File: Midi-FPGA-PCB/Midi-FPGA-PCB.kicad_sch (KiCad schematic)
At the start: 18 parts, among them Q1 DMP2123L, SW1 Reset, U1 ESP32-WROOM-32, U2 AP7361EA

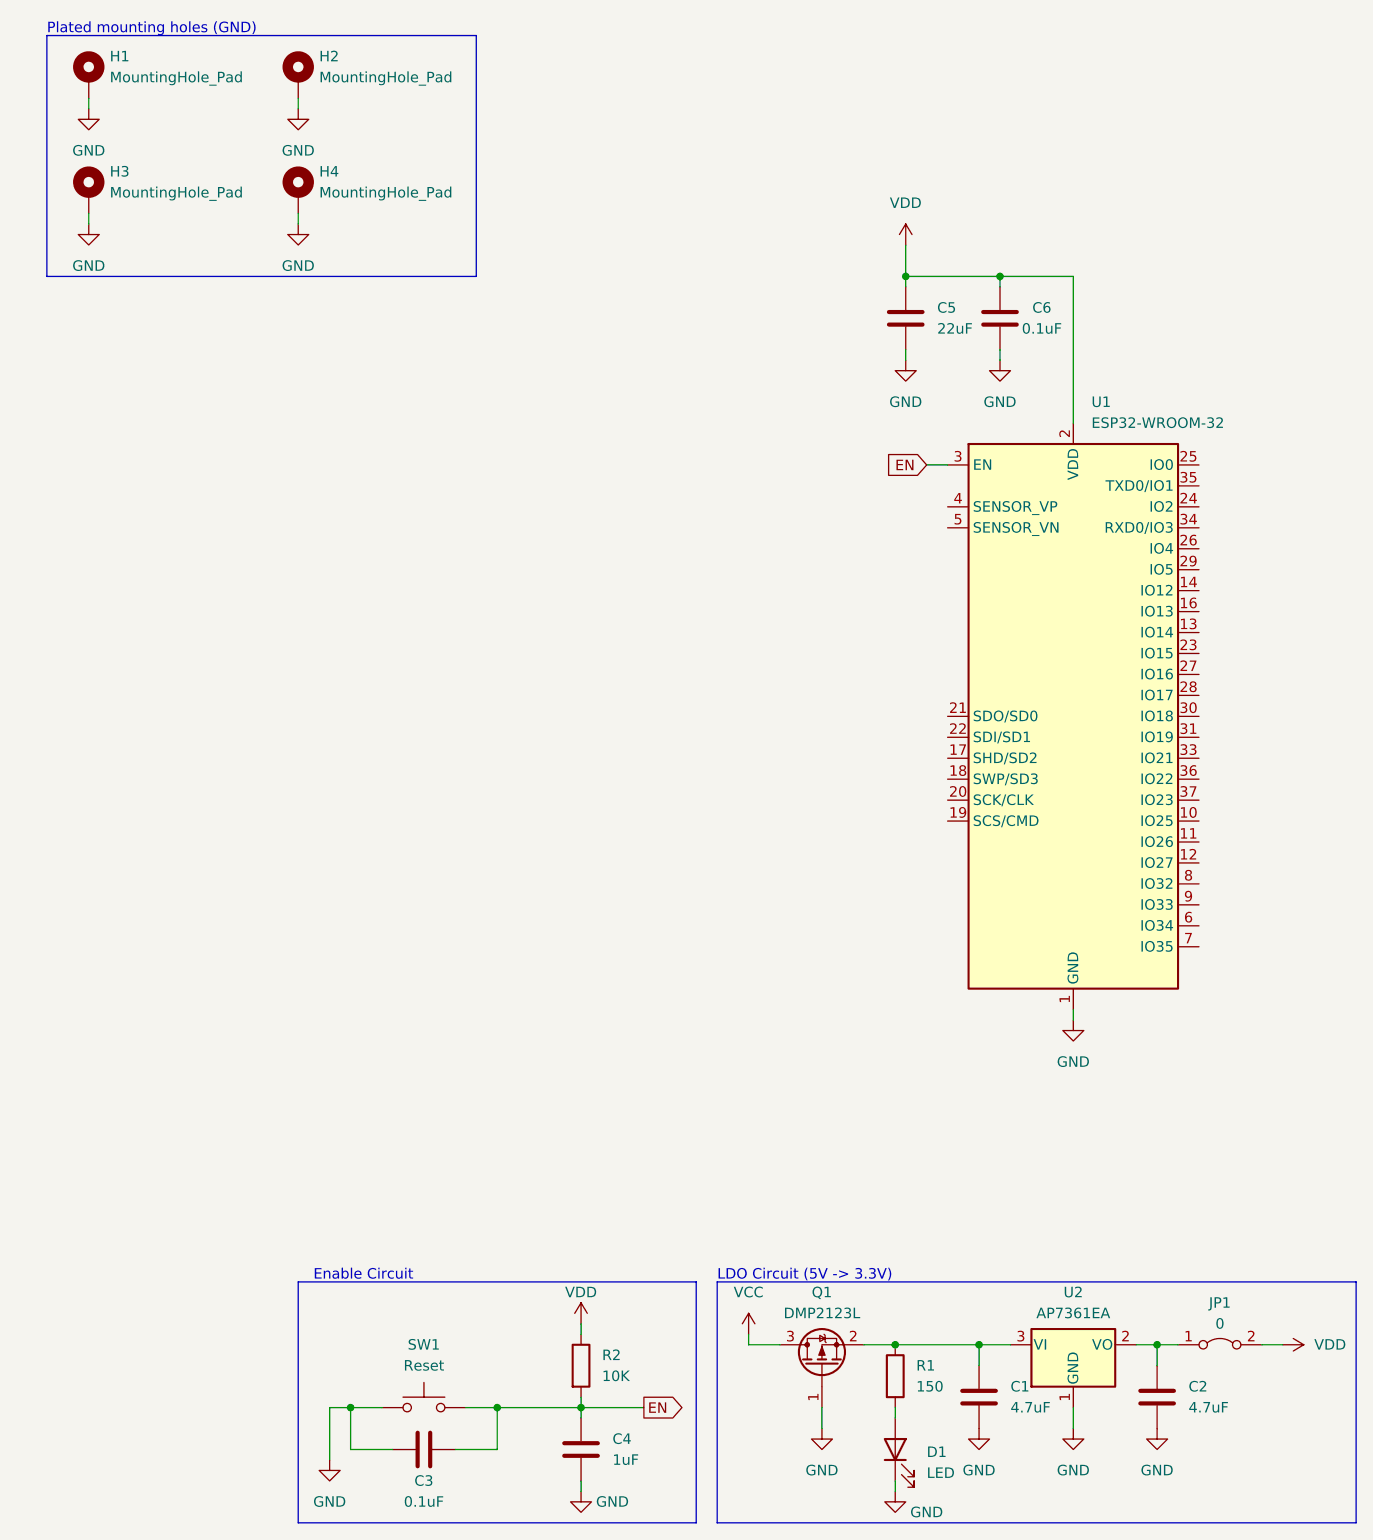
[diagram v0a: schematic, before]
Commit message: Created boot mode circuit
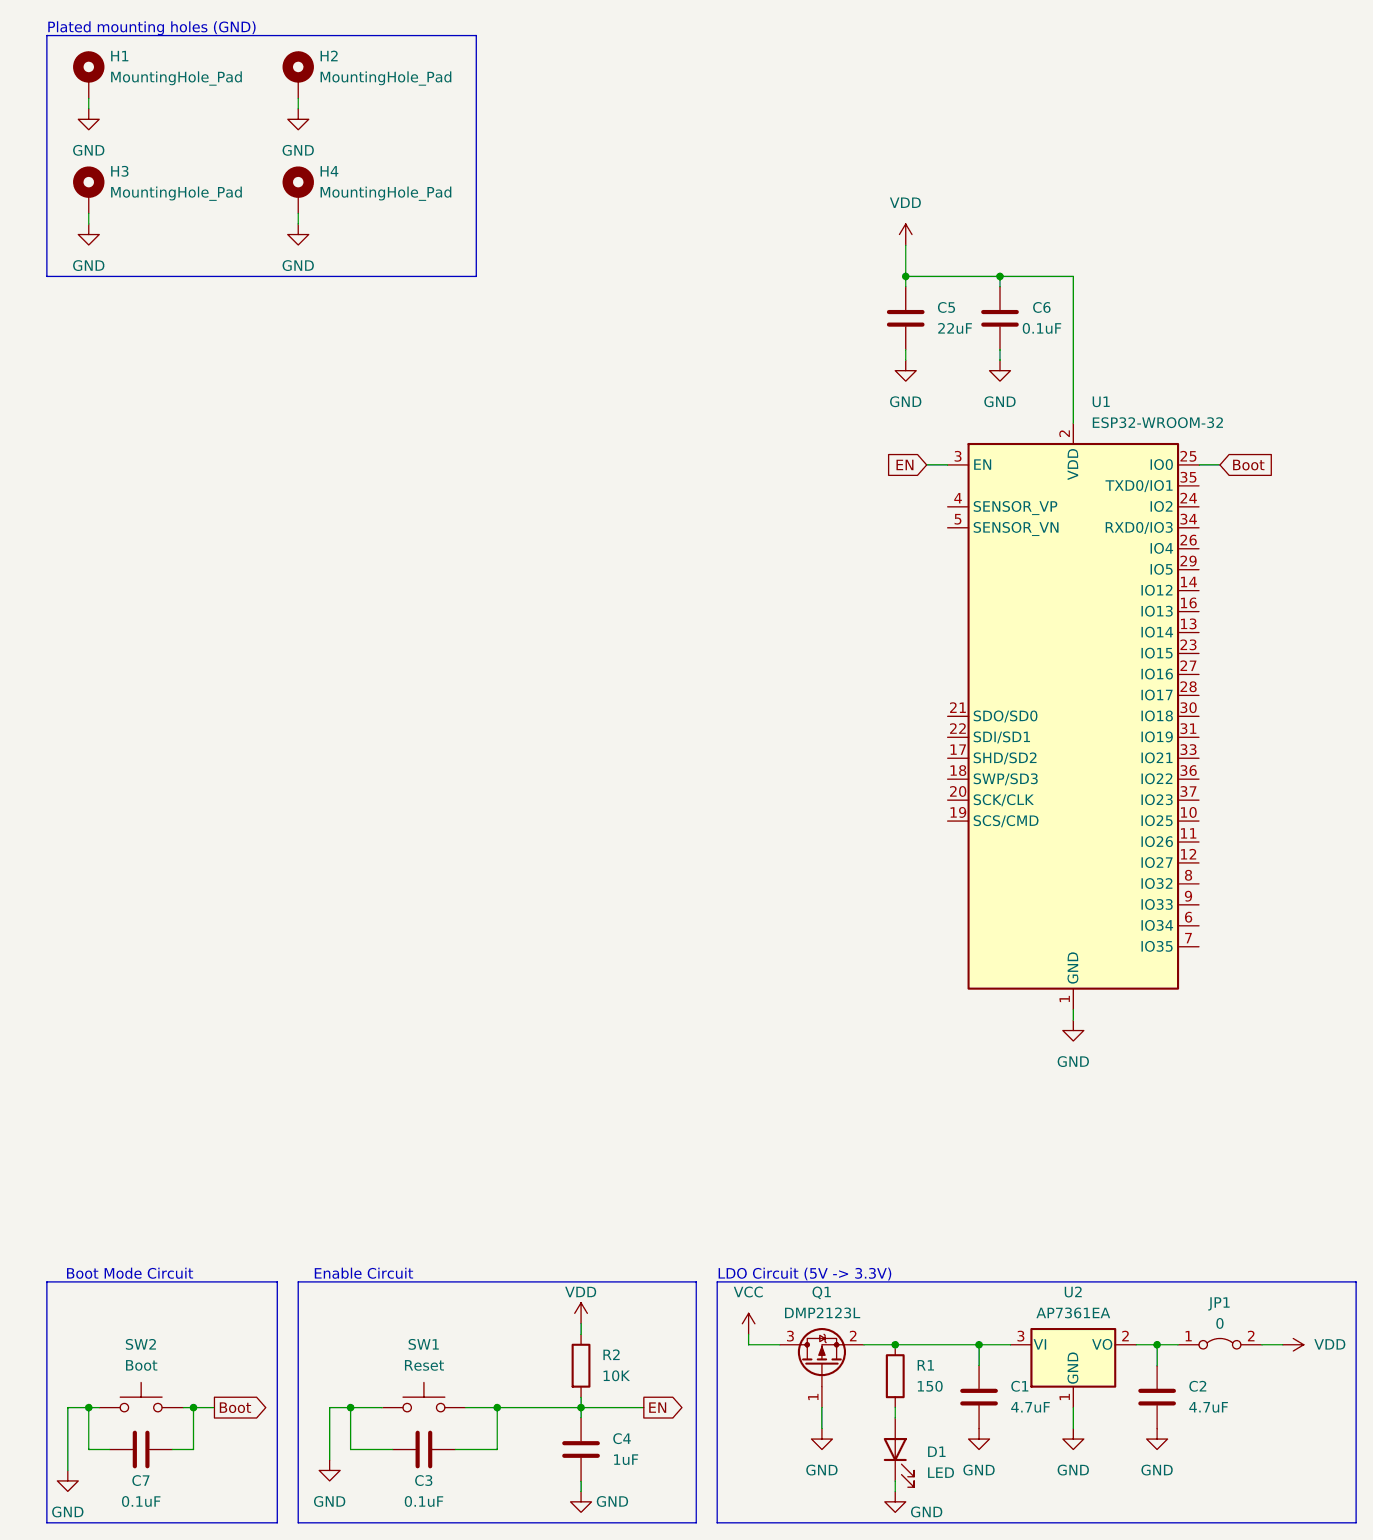
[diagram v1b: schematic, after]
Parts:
- added C7: 0.1uF, Capacitor_SMD:C_0805_2012Metric_Pad1.18x1.45mm_HandSolder, symbol Device:C
- added SW2: Boot, symbol Switch:SW_Push
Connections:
- net GND: now also C7.1, SW2.1
- net Boot: now reaches U1.25 (IO0)
- net Boot: now also C7.2, SW2.2
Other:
- note added: "Boot Mode Circuit"
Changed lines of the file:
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@@
   (junction (at 130.81 44.45) (diameter 0) (color 0 0 0 0)
   )
+  (junction (at 33.02 181.61) (diameter 0) (color 0 0 0 0)
+  )
   (junction (at 80.01 181.61) (diameter 0) (color 0 0 0 0)
   )
@@
   (junction (at 69.85 181.61) (diameter 0) (color 0 0 0 0)
   )
+  (junction (at 20.32 181.61) (diameter 0) (color 0 0 0 0)
+  )
   (wire (pts (xy 118.11 173.99) (xy 128.27 173.99))
     (stroke (width 0) (type default))
@@
     (stroke (width 0) (type default))
   )
+  (wire (pts (xy 30.48 186.69) (xy 33.02 186.69))
+    (stroke (width 0) (type default))
+  )
   (wire (pts (xy 149.86 173.99) (xy 149.86 176.53))
     (stroke (width 0) (type default))
@@
     (stroke (width 0) (type default))
   )
+  (wire (pts (xy 21.59 181.61) (xy 20.32 181.61))
+    (stroke (width 0) (type default))
+  )
   (wire (pts (xy 80.01 180.34) (xy 80.01 181.61))
     (stroke (width 0) (type default))
@@
     (stroke (width 0) (type default))
   )
+  (wire (pts (xy 20.32 186.69) (xy 20.32 181.61))
+    (stroke (width 0) (type default))
+  )
+  (wire (pts (xy 154.94 67.31) (xy 157.48 67.31))
+    (stroke (width 0) (type default))
+  )
   (wire (pts (xy 66.04 181.61) (xy 69.85 181.61))
     (stroke (width 0) (type default))
@@
     (stroke (width 0) (type default))
   )
+  (wire (pts (xy 31.75 181.61) (xy 33.02 181.61))
+    (stroke (width 0) (type default))
+  )
   (wire (pts (xy 64.77 186.69) (xy 69.85 186.69))
     (stroke (width 0) (type default))
@@
     (stroke (width 0) (type default))
   )
+  (wire (pts (xy 33.02 181.61) (xy 35.56 181.61))
+    (stroke (width 0) (type default))
+  )
   (wire (pts (xy 128.27 173.99) (xy 132.08 173.99))
     (stroke (width 0) (type default))
   )
+  (wire (pts (xy 20.32 181.61) (xy 17.78 181.61))
+    (stroke (width 0) (type default))
+  )
   (wire (pts (xy 147.32 173.99) (xy 149.86 173.99))
     (stroke (width 0) (type default))
@@
     (stroke (width 0) (type default))
   )
+  (wire (pts (xy 17.78 181.61) (xy 17.78 189.23))
+    (stroke (width 0) (type default))
+  )
   (wire (pts (xy 114.3 173.99) (xy 118.11 173.99))
     (stroke (width 0) (type default))
@@
     (stroke (width 0) (type default))
   )
+  (wire (pts (xy 22.86 186.69) (xy 20.32 186.69))
+    (stroke (width 0) (type default))
+  )
+  (wire (pts (xy 33.02 186.69) (xy 33.02 181.61))
+    (stroke (width 0) (type default))
+  )
   (wire (pts (xy 45.72 22.86) (xy 45.72 24.13))
     (stroke (width 0) (type default))
@@
     (fill (type none))
   )
+  (rectangle (start 15.24 166.37) (end 43.18 195.58)
+    (stroke (width 0) (type default))
+    (fill (type none))
+  )
   (rectangle (start 45.72 166.37) (end 93.98 195.58)
     (stroke (width 0) (type default))
@@
     (stroke (width 0) (type default))
     (fill (type none))
+  )
+  (text "Boot Mode Circuit" (at 33.02 166.37 0)
+    (effects (font (size 1.27 1.27)) (justify right bottom))
   )
   (text "Plated mounting holes (GND)" (at 15.24 15.24 0)
@@
   (text "Enable Circuit" (at 59.69 166.37 0)
     (effects (font (size 1.27 1.27)) (justify right bottom))
+  )
+  (global_label "Boot" (shape output) (at 35.56 181.61 0) (fields_autoplaced)
+    (effects (font (size 1.27 1.27)) (justify left))
+    (property "Intersheetrefs" "${INTERSHEET_REFS}" (at 42.8389 181.61 0)
+      (effects (font (size 1.27 1.27)) (justify left) hide)
+    )
   )
   (global_label "EN" (shape input) (at 121.92 67.31 180) (fields_autoplaced)
@@
     )
   )
+  (global_label "Boot" (shape input) (at 157.48 67.31 0) (fields_autoplaced)
+    (effects (font (size 1.27 1.27)) (justify left))
+    (property "Intersheetrefs" "${INTERSHEET_REFS}" (at 164.7589 67.31 0)
+      (effects (font (size 1.27 1.27)) (justify left) hide)
+    )
+  )
   (symbol (lib_id "power:GND") (at 130.81 54.61 0) (unit 1)
     (in_bom yes) (on_board yes) (dnp no) (fields_autoplaced)
@@
         (path "/75ad38e9-b0d3-45bc-bcac-026c9800f4ea"
           (reference "SW1") (unit 1)
+        )
+      )
+    )
+  )
+  (symbol (lib_id "Switch:SW_Push") (at 26.67 181.61 0) (unit 1)
+    (in_bom yes) (on_board yes) (dnp no) (fields_autoplaced)
+    (property "Reference" "SW2" (at 26.67 173.99 0)
+      (effects (font (size 1.27 1.27)))
+    )
+    (property "Value" "Boot" (at 26.67 176.53 0)
+      (effects (font (size 1.27 1.27)))
+    )
+    (property "Footprint" "" (at 26.67 176.53 0)
+      (effects (font (size 1.27 1.27)) hide)
+    )
+    (property "Datasheet" "https://www.ckswitches.com/media/2728/pts815.pdf" (at 26.67 176.53 0)
+      (effects (font (size 1.27 1.27)) hide)
+    )
+    (property "URL" "https://www.digikey.co.uk/en/products/detail/c-k/PTS815-SJM-250-SMTR-LFS/9947846" (at 26.67 181.61 0)
+      (effects (font (size 1.27 1.27)) hide)
+    )
+    (pin "1")
+    (pin "2")
+    (instances
+      (project "Midi-FPGA-PCB"
+        (path "/75ad38e9-b0d3-45bc-bcac-026c9800f4ea"
+          (reference "SW2") (unit 1)
         )
       )
@@
     )
   )
+  (symbol (lib_id "power:GND") (at 17.78 189.23 0) (unit 1)
+    (in_bom yes) (on_board yes) (dnp no) (fields_autoplaced)
+    (property "Reference" "#PWR019" (at 17.78 195.58 0)
+      (effects (font (size 1.27 1.27)) hide)
+    )
+    (property "Value" "GND" (at 17.78 194.31 0)
+      (effects (font (size 1.27 1.27)))
+    )
+    (property "Footprint" "" (at 17.78 189.23 0)
+      (effects (font (size 1.27 1.27)) hide)
+    )
+    (property "Datasheet" "" (at 17.78 189.23 0)
+      (effects (font (size 1.27 1.27)) hide)
+    )
+    (pin "1")
+    (instances
+      (project "Midi-FPGA-PCB"
+        (path "/75ad38e9-b0d3-45bc-bcac-026c9800f4ea"
+          (reference "#PWR019") (unit 1)
+        )
+      )
+    )
+  )
   (symbol (lib_id "Device:Q_PMOS_GSD") (at 109.22 176.53 90) (unit 1)
     (in_bom yes) (on_board yes) (dnp no) (fields_autoplaced)
@@
         )
       )
+    )
+  )
+  (symbol (lib_id "Device:C") (at 26.67 186.69 90) (unit 1)
+    (in_bom yes) (on_board yes) (dnp no)
+    (property "Reference" "C7" (at 26.67 190.5 90)
+      (effects (font (size 1.27 1.27)))
+    )
+    (property "Value" "0.1uF" (at 26.67 193.04 90)
+      (effects (font (size 1.27 1.27)))
+    )
+    (property "Footprint" "Capacitor_SMD:C_0805_2012Metric_Pad1.18x1.45mm_HandSolder" (at 30.48 185.7248 0)
+      (effects (font (size 1.27 1.27)) hide)
+    )
+    (property "Datasheet" "https://mm.digikey.com/Volume0/opasdata/d220001/medias/docus/609/CL21B104KBCNNN_Spec.pdf" (at 26.67 186.69 0)
+      (effects (font (size 1.27 1.27)) hide)
+    )
+    (property "URL" "https://www.digikey.co.uk/en/products/detail/samsung-electro-mechanics/CL21B104KBCNNNC/3886661" (at 26.67 186.69 90)
+      (effects (font (size 1.27 1.27)) hide)
+    )
+    (pin "1")
+    (pin "2")
+    (instances
+      (project "Midi-FPGA-PCB"
+        (path "/75ad38e9-b0d3-45bc-bcac-026c9800f4ea"
+          (reference "C7") (unit 1)
+        )
+      )

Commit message: Reset annotations
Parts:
- renumbered C5 to C1, C6 to C2, C1 to C3, C2 to C4, C7 to C5, C3 to C6, C4 to C7, R2 to R1, R1 to R2, SW2 to SW1, SW1 to SW2
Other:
- moved on the sheet: C4, JP1, U2
